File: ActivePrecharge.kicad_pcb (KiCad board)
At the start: 2 copper layers, 36 parts, among them J1 Conn_01x02, J2 Conn_01x03, J3 Conn_01x02, Q1 IRLML0030, U1 TCMT1106, U2 NCP785AH120T1G, U3 NCP785AH120T1G

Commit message: ACPR_Initial_Layout_Jacob
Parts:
- removed R1a1: 10k, Resistor_SMD:R_0805_2012Metric
- removed R6a1: 250, Resistor_SMD:R_0805_2012Metric
- C3, C5: footprint Capacitor_SMD:C_0805_2012Metric -> BigCap:CAPC5750X220N
- R1: renamed from R1b1; value 100k -> 110k; footprint Resistor_SMD:R_0805_2012Metric -> Resistor_SMD:R_1206_3216Metric
- R3: footprint Resistor_SMD:R_0805_2012Metric -> Resistor_SMD:R_1206_3216Metric
- R6b1: value 500 -> 750
- moved H4 126.5 mm to (85.8, 115.5)
- moved H2 80.8 mm to (139.5, 75.5)
- moved Q1 69.0 mm to (134.1, 108.4), turned to 90 degrees
- moved J3 65.9 mm to (138.8, 100.0), turned to -90 degrees
- moved D3 64.5 mm to (133.7, 77.5), turned to -90 degrees
- moved D1 62.4 mm to (133.5, 101.7), turned to -90 degrees
- moved R11 61.7 mm to (130.5, 110.2), turned to -90 degrees
- moved J1 57.6 mm to (138.7, 87.0), turned to -90 degrees
- moved PreResH1 56.3 mm to (85.8, 75.8)
- moved H3 55.6 mm to (139.5, 115.5)
- moved D2 52.4 mm to (133.8, 96.4), turned to 90 degrees
- moved R9 52.0 mm to (133.8, 92.4), turned to 90 degrees
- moved C2 48.0 mm to (133.7, 84.8), turned to -90 degrees
- moved C1 47.5 mm to (133.7, 88.5), turned to 90 degrees
- moved R10 46.5 mm to (133.7, 81.2), turned to 90 degrees
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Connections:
- J1 pad 1: +12V -> LVGND
- J1 pad 2: LVGND -> +12V
- J2 pad 1: /HVRef -> HVGND
- J2 pad 2: /HVIn -> /HVRef
- J2 pad 3: HVGND -> /HVIn
- R1 pad 1: Net-(R1a1-Pad2) -> /HVRef
- R6b1 pad 1: Net-(R6a1-Pad2) -> /Vcc
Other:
- board outline added: 64.2 x 50.5 mm

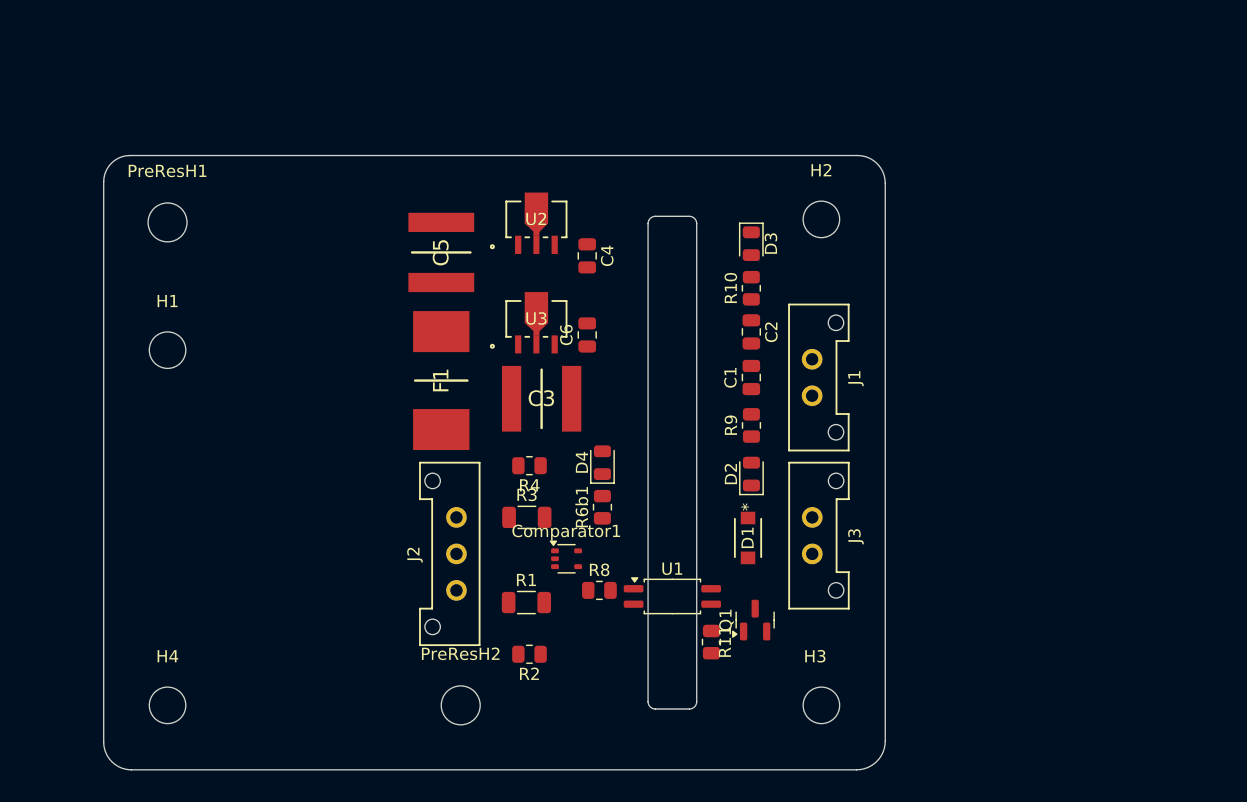
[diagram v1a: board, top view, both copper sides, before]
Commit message: schematic edits and layout prototype
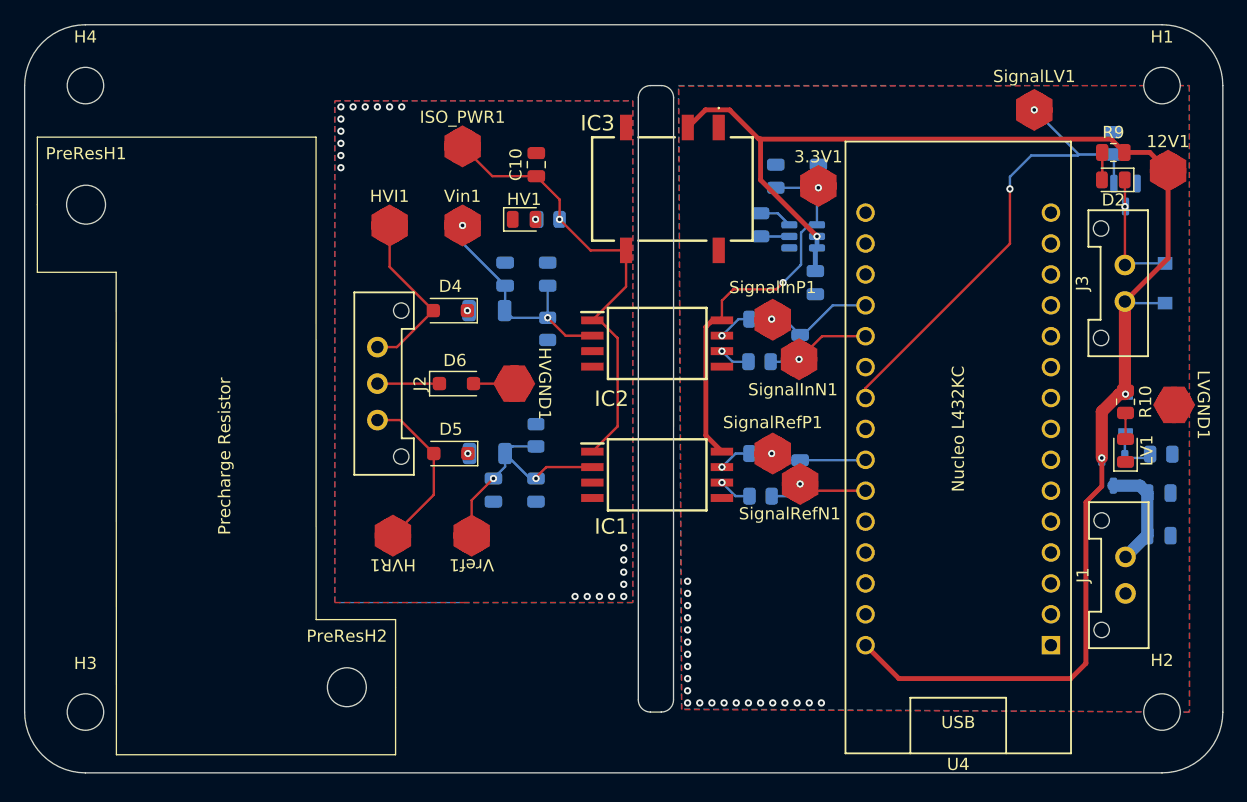
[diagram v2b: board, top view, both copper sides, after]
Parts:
- removed Comparator1: TLV9301xDCK, Package_TO_SOT_SMD:SOT-353_SC-70-5
- removed D3: LED, LED_SMD:LED_0805_2012Metric
- removed F1: 46205, 46205Fuse:FUSC10545X460N
- removed R6b1: 750, Resistor_SMD:R_0805_2012Metric
- removed U1: TCMT1106, Package_SO:SOP-4_4.4x2.6mm_P1.27mm
- removed U2: NCP785AH120T1G, LDO:SOT-89-3_2P7X4P7_ONS
- added 12V1: TestPoint, Active-PrechargeLib:TestPoint_HEX_3mmID, F.Cu at (168.0, 71.5)
- added 3.3V1: TestPoint, Active-PrechargeLib:TestPoint_HEX_3mmID, F.Cu at (139.2, 72.8)
- added C10: 0.1u, Capacitor_SMD:C_0805_2012Metric, F.Cu at (116.1, 71.0)
- added C12: 10n, Capacitor_SMD:C_0805_2012Metric, B.Cu at (137.8, 96.2)
- added C13: 100n, Capacitor_SMD:C_0805_2012Metric, B.Cu at (139.2, 72.0)
- added C15: 1uF, Capacitor_SMD:C_0805_2012Metric, B.Cu at (113.5, 80.0)
- added C7: 1uF, Capacitor_SMD:C_0805_2012Metric, B.Cu at (112.5, 97.8)
- added C8: 10n, Capacitor_SMD:C_0805_2012Metric, B.Cu at (137.8, 86.0)
- added C9: 100p, Capacitor_SMD:C_0805_2012Metric, B.Cu at (116.0, 97.8)
- added D5: RSX068MP2STR, Diode_SMD:D_SOD-123F, F.Cu at (109.0, 94.8)
- added D6: RSX068MP2STR, Diode_SMD:D_SOD-123F, F.Cu at (109.5, 89.0)
- added D7: BZT52-B12-QX, Active-PrechargeLib:BZT52B12QX, B.Cu at (164.5, 91.5)
- added HV1: LED, LED_SMD:LED_0805_2012Metric, F.Cu at (115.1, 75.5)
- added HVGND1: TestPoint, Active-PrechargeLib:TestPoint_HEX_3mmID, F.Cu at (114.2, 89.0)
- added HVI1: TestPoint, Active-PrechargeLib:TestPoint_HEX_3mmID, F.Cu at (104.0, 76.0)
- added HVR1: TestPoint, Active-PrechargeLib:TestPoint_HEX_3mmID, F.Cu at (104.3, 101.5)
- added IC1: AMC1311BDWVR, AMC1311:SOIC127P1150X280-8N, F.Cu at (126.0, 96.5)
- added IC2: AMC1311BDWVR, AMC1311:SOIC127P1150X280-8N, F.Cu at (126.0, 85.7)
- added IC3: 1769205241, Active-PrechargeLib:1769205241, F.Cu at (127.2, 73.0)
- added ISO_PWR1: TestPoint, utsvt-special:TestPoint_HEX_3mmID, F.Cu at (110.0, 69.5)
- added LV1: LED, LED_SMD:LED_0805_2012Metric, F.Cu at (164.5, 94.5)
- added LVGND1: TestPoint, Active-PrechargeLib:TestPoint_HEX_3mmID, F.Cu at (168.5, 90.8)
- added Q2: PMV35EPER, Package_TO_SOT_SMD:SOT-23-3, B.Cu at (163.5, 96.2)
- added R12: 100k, Resistor_SMD:R_0805_2012Metric, B.Cu at (167.4, 94.8)
- added R13: 640, Resistor_SMD:R_0805_2012Metric, B.Cu at (117.1, 75.5)
- added R5: 10, Resistor_SMD:R_0805_2012Metric, B.Cu at (134.5, 83.7)
- added R6: 10, Resistor_SMD:R_0805_2012Metric, B.Cu at (134.4, 87.2)
- added R7: 10, Resistor_SMD:R_0805_2012Metric, B.Cu at (134.5, 94.8)
- added SignalInN1: TestPoint, Active-PrechargeLib:TestPoint_HEX_3mmID, F.Cu at (137.7, 87.0)
- added SignalInP1: TestPoint, Active-PrechargeLib:TestPoint_HEX_3mmID, F.Cu at (135.5, 83.8)
- added SignalLV1: TestPoint, Active-PrechargeLib:TestPoint_HEX_3mmID, F.Cu at (157.0, 66.5)
- added SignalRefN1: TestPoint, Active-PrechargeLib:TestPoint_HEX_3mmID, F.Cu at (137.8, 97.2)
- added SignalRefP1: TestPoint, Active-PrechargeLib:TestPoint_HEX_3mmID, F.Cu at (135.5, 94.8)
- added U4: Nucleo_L432KC, utsvt-special:NucleoL432KC, F.Cu at (150.8, 92.7)
- added Vin1: TestPoint, Active-PrechargeLib:TestPoint_HEX_3mmID, F.Cu at (110.0, 76.0)
- added Vref1: TestPoint, Active-PrechargeLib:TestPoint_HEX_3mmID, F.Cu at (110.8, 101.5)
- C1, C2: value 100u -> 10u; moved to B.Cu
- C3: value 2.2u -> 100p; footprint BigCap:CAPC5750X220N -> Capacitor_SMD:C_0805_2012Metric; moved to B.Cu
- C4: value 22u -> 100n; moved to B.Cu
- C5: value 2.2u -> 44u; footprint BigCap:CAPC5750X220N -> Capacitor_SMD:C_0805_2012Metric; moved to B.Cu
- C6: value 22u -> 10u; moved to B.Cu
- D1, Q1, R11, R3: moved to B.Cu
- D4: value LED -> RSX068MP2STR; footprint LED_SMD:LED_0805_2012Metric -> Diode_SMD:D_SOD-123F
- R1: value 110k -> 100k; moved to B.Cu
- R10: value 5k -> 2k
- R2, R4: value 1k -> 2k; moved to B.Cu
- R8: value 250 -> 10; moved to B.Cu
- U3: value NCP785AH120T1G -> AP63203WU; footprint LDO:SOT-89-3_2P7X4P7_ONS -> Package_TO_SOT_SMD:TSOT-23-6; moved to B.Cu
- moved H1 84.6 mm to (167.5, 64.5)
- moved H3 60.5 mm to (79.0, 116.0)
- moved R11 52.7 mm to (163.5, 69.2), turned to 90 degrees
- moved H4 51.4 mm to (79.0, 64.5)
- moved H2 49.2 mm to (167.5, 116.0)
- moved Q1 46.3 mm to (164.5, 73.5), turned to -90 degrees
- moved D1 40.2 mm to (167.8, 80.8), turned to 90 degrees
- moved D2 38.3 mm to (163.5, 72.2), turned to 180 degrees
- moved R9 37.3 mm to (163.5, 70.0), turned to 0 degrees
- moved C2 36.0 mm to (167.2, 98.0), turned to 0 degrees
- moved C1 35.9 mm to (167.2, 101.5), turned to 0 degrees
- moved J1 32.2 mm to (164.5, 106.2), turned to 90 degrees
- moved R10 32.1 mm to (164.5, 90.5), turned to -90 degrees
- moved J3 31.2 mm to (164.4, 82.2), turned to 90 degrees
- moved C5 28.2 mm to (135.8, 72.0)
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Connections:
- C3 pad 1: Net-(U2-IN) -> /HVGND
- C3 pad 2: HVGND -> /Vin
- C4 pad 1: /Vcc -> Net-(U3-SW)
- C4 pad 2: HVGND -> Net-(U3-BST)
- C5 pad 1: Net-(U2-IN) -> /3.3V
- C5 pad 2: HVGND -> LVGND
- C6 pad 1: /Vcc -> LVGND
- C6 pad 2: HVGND -> /LV+
- D1 pad 1: +12V -> /LV+
- D4 pad 1: HVGND -> /HVIn
- D4 pad 2: Net-(D4-A) -> /HIn
- J2 pad 1: HVGND -> /HIn
- J2 pad 2: /HVRef -> HGND
- J2 pad 3: /HVIn -> HRef
- J3 pad 1: +12V -> /LV+
- R10 pad 1: +12V -> /LV+
- R2 pad 2: HVGND -> /HVGND
- R4 pad 2: HVGND -> /HVGND
- R8 pad 1: /SignalHV -> Net-(IC1-VOUTN)
- R8 pad 2: Net-(R8-Pad2) -> /SignalRefN
- R9 pad 2: +12V -> /LV+
- U3 pad 1: Net-(U2-IN) -> /3.3V
- U3 pad 2: HVGND -> /LV+
- U3 pad 3: /Vcc -> /LV+
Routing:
- net /LV+: track 0.00 -> 121.5 mm, vias 0 -> 3
- net /SignalLV: track 0.00 -> 40.0 mm, vias 0 -> 2
- net /ISO_PWR: track 0.00 -> 37.7 mm, vias 0 -> 1
- net /3.3V: track 0.00 -> 32.5 mm, vias 0 -> 2
- net /Vin: track 0.00 -> 19.2 mm, vias 0 -> 2
- net /Vref: track 0.00 -> 19.1 mm, vias 0 -> 2
- net /HIn: track 0.00 -> 14.3 mm
- net HRef: track 0.00 -> 13.9 mm
- net Net-(D1-A): track 0.00 -> 10.4 mm, vias 0 -> 1
- net /SignalInP: track 0.00 -> 9.26 mm, vias 0 -> 1
- net +12V: track 0.00 -> 9.13 mm
- net /SignalInN: track 0.00 -> 8.67 mm, vias 0 -> 1
- net /SignalRefN: track 0.00 -> 8.38 mm, vias 0 -> 1
- net /SignalRefP: track 0.00 -> 7.96 mm, vias 0 -> 1
- net HGND: track 0.00 -> 5.10 mm
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- added copper zone on B.Cu, net /HVGND
- added copper zone on F.Cu, net /HVGND
- added copper zone on B.Cu, net LVGND
- added copper zone on F.Cu, net LVGND
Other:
- board size 64.2 x 50.5 mm -> 98.5 x 61.5 mm
- board text added: "Precharge Resistor"

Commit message: balancing
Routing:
- net /3.3V: track 32.5 -> 33.9 mm
- net LVGND: vias 22 -> 29
- net /HVGND: vias 20 -> 29
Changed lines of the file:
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@@
+	)
+	(via
+		(at 156.5 109.25)
+		(size 0.6)
+		(drill 0.3)
+		(layers "F.Cu" "B.Cu")
+		(free yes)
+		(net 2)
 	)
 	(via
@@
 	)
 	(via
+		(at 156.5 107.25)
+		(size 0.6)
+		(drill 0.3)
+		(layers "F.Cu" "B.Cu")
+		(free yes)
+		(net 2)
+	)
+	(via
 		(at 128.5 113.25)
 		(size 0.6)
@@
 	)
 	(via
+		(at 156.5 108.25)
+		(size 0.6)
+		(drill 0.3)
+		(layers "F.Cu" "B.Cu")
+		(free yes)
+		(net 2)
+	)
+	(via
 		(at 128.5 108.25)
 		(size 0.6)
@@
 	)
 	(via
+		(at 156.5 105.25)
+		(size 0.6)
+		(drill 0.3)
+		(layers "F.Cu" "B.Cu")
+		(free yes)
+		(net 2)
+	)
+	(via
 		(at 132.5 115.25)
 		(size 0.6)
@@
 	)
 	(via
+		(at 156.5 106.25)
+		(size 0.6)
+		(drill 0.3)
+		(layers "F.Cu" "B.Cu")
+		(free yes)
+		(net 2)
+	)
+	(via
+		(at 156.5 111.25)
+		(size 0.6)
+		(drill 0.3)
+		(layers "F.Cu" "B.Cu")
+		(free yes)
+		(net 2)
+	)
+	(via
 		(at 130.5 115.25)
 		(size 0.6)
@@
 	(via
 		(at 136.5 115.25)
+		(size 0.6)
+		(drill 0.3)
+		(layers "F.Cu" "B.Cu")
+		(free yes)
+		(net 2)
+	)
+	(via
+		(at 156.5 110.25)
 		(size 0.6)
 		(drill 0.3)
@@
 	)
 	(via
+		(at 100 106.5)
+		(size 0.6)
+		(drill 0.3)
+		(layers "F.Cu" "B.Cu")
+		(free yes)
+		(net 11)
+	)
+	(via
 		(at 100 69.25)
 		(size 0.6)
@@
 	)
 	(via
+		(at 102 106.5)
+		(size 0.6)
+		(drill 0.3)
+		(layers "F.Cu" "B.Cu")
+		(free yes)
+		(net 11)
+	)
+	(via
 		(at 100 66.25)
 		(size 0.6)
@@
 	)
 	(via
+		(at 100 103.5)
+		(size 0.6)
+		(drill 0.3)
+		(layers "F.Cu" "B.Cu")
+		(free yes)
+		(net 11)
+	)
+	(via
+		(at 100 102.5)
+		(size 0.6)
+		(drill 0.3)
+		(layers "F.Cu" "B.Cu")
+		(free yes)
+		(net 11)
+	)
+	(via
+		(at 100 105.5)
+		(size 0.6)
+		(drill 0.3)
+		(layers "F.Cu" "B.Cu")
+		(free yes)
+		(net 11)
+	)
+	(via
 		(at 104 66.25)
 		(size 0.6)
@@
 	)
 	(via
+		(at 103 106.5)
+		(size 0.6)
+		(drill 0.3)
+		(layers "F.Cu" "B.Cu")
+		(free yes)
+		(net 11)
+	)
+	(via
 		(at 119.25 106.5)
 		(size 0.6)
@@
 	)
 	(via
+		(at 104 106.5)
+		(size 0.6)
+		(drill 0.3)
+		(layers "F.Cu" "B.Cu")
+		(free yes)
+		(net 11)
+	)
+	(via
 		(at 102 66.25)
 		(size 0.6)
@@
 	)
 	(via
+		(at 101 106.5)
+		(size 0.6)
+		(drill 0.3)
+		(layers "F.Cu" "B.Cu")
+		(free yes)
+		(net 11)
+	)
+	(via
 		(at 123.25 106.5)
 		(size 0.6)
@@
 	(via
 		(at 121.25 106.5)
+		(size 0.6)
+		(drill 0.3)
+		(layers "F.Cu" "B.Cu")
+		(free yes)
+		(net 11)
+	)
+	(via
+		(at 100 104.5)
 		(size 0.6)
 		(drill 0.3)
@@
 	)
 	(segment
-		(start 130 84.34)
-		(end 130 93.27)
-		(width 0.4)
-		(layer "F.Cu")
-		(net 14)
-	)
-	(segment
 		(start 132.25 81.25)
 		(end 131.325 82.175)
@@
 	)
 	(segment
-		(start 130.545 83.795)
-		(end 130 84.34)
-		(width 0.4)
-		(layer "F.Cu")
-		(net 14)
-	)
-	(segment
 		(start 131.325 82.175)
 		(end 131.325 83.795)
@@
 	)
 	(segment
+		(start 130.055 83.795)
+		(end 128.7 85.15)
+		(width 0.2)
+		(layer "F.Cu")
+		(net 14)
+	)
+	(segment
+		(start 128.7 91.97)
+		(end 131.325 94.595)
+		(width 0.2)
+		(layer "F.Cu")
+		(net 14)
+	)
+	(segment
+		(start 128.7 85.15)
+		(end 128.7 91.97)
+		(width 0.2)
+		(layer "F.Cu")
+		(net 14)
+	)
+	(segment
 		(start 136.35 80.7)
 		(end 135.8 81.25)
@@
 	)
 	(segment
-		(start 130 93.27)
-		(end 131.325 94.595)
-		(width 0.4)
+		(start 131.325 83.795)
+		(end 130.055 83.795)
+		(width 0.2)
 		(layer "F.Cu")
 		(net 14)
-	)
-	(segment
-		(start 131.325 83.795)
-		(end 130.545 83.795)
-		(width 0.4)
-		(layer "F.Cu")
-		(net 14)

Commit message: layout revisions inital draft finished
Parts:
- C10: moved to B.Cu
- R13: moved to F.Cu
- moved HVGND1 15.5 mm to (113.5, 104.5), turned to 180 degrees
- moved C3 8.05 mm to (113.5, 87.2), turned to 90 degrees
- moved C4 8.00 mm to (126.6, 74.6)
- moved C5 8.00 mm to (127.9, 70.6)
- moved C12 7.73 mm to (130.1, 97.2)
- moved R7 7.73 mm to (126.8, 95.8)
- moved R8 7.73 mm to (126.8, 99.2)
- moved C13 7.68 mm to (131.9, 69.8)
- moved C6 7.68 mm to (131.6, 78.6)
- moved U3 7.68 mm to (130.6, 74.8)
- moved 3.3V1 7.58 mm to (131.9, 70.9)
- moved C8 7.51 mm to (130.2, 86.3)
- moved R5 7.51 mm to (127.0, 84.0)
- moved R6 7.51 mm to (126.9, 87.5)
- moved SignalInN1 7.51 mm to (130.2, 87.3)
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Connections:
- D6 pad 2: Net-(D6-A) -> /HVGND
- HVGND1 pad 1: Net-(D6-A) -> /HVGND
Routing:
- net /LV+: track 121.5 -> 111.1 mm
- net /SignalRefN: track 8.38 -> 18.6 mm, vias 1 -> 0
- net Net-(D1-A): track 10.4 -> 15.7 mm, vias 1 -> 0
- net /SignalLV: track 40.0 -> 34.8 mm, vias 2 -> 1
- net +12V: track 9.13 -> 12.9 mm
- net /3.3V: track 33.9 -> 37.4 mm, vias 2 -> 1
- net Net-(D6-A): track 3.35 -> 0.00 mm
- net Net-(D7-A): track 3.93 -> 5.75 mm
- net /ISO_PWR: track 37.7 -> 36.0 mm
- net Net-(HV1-A): track 0.00 -> 1.65 mm, vias 1 -> 0
- net /SignalRefP: track 7.96 -> 9.59 mm
- net Net-(IC2-VOUTP): track 2.83 -> 1.38 mm
- net Net-(IC1-VOUTP): track 2.72 -> 1.36 mm
- net Net-(IC1-VOUTN): track 2.72 -> 1.36 mm
- net /SignalInP: track 9.26 -> 10.5 mm
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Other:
- board size 98.5 x 61.5 mm -> 93.5 x 61.5 mm

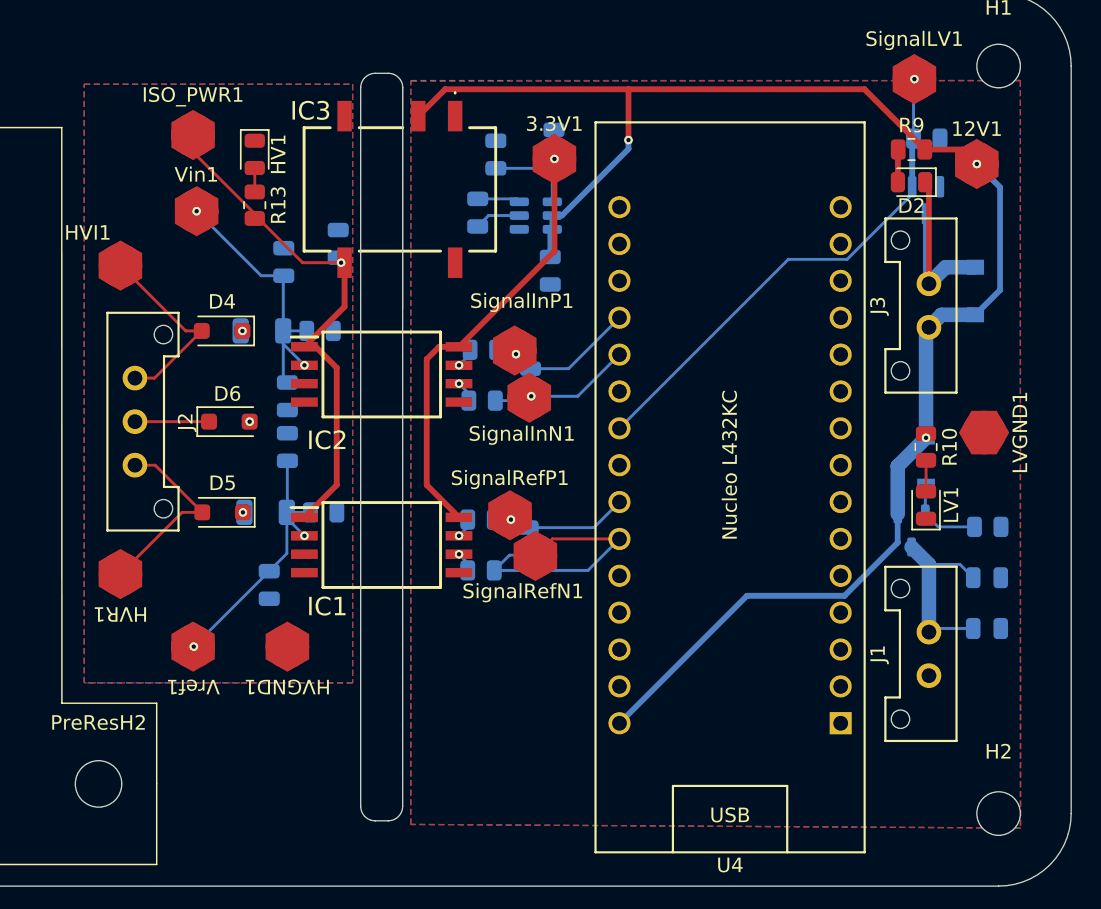
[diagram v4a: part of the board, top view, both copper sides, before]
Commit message: added stitching vias and fixed silkscreen warnings
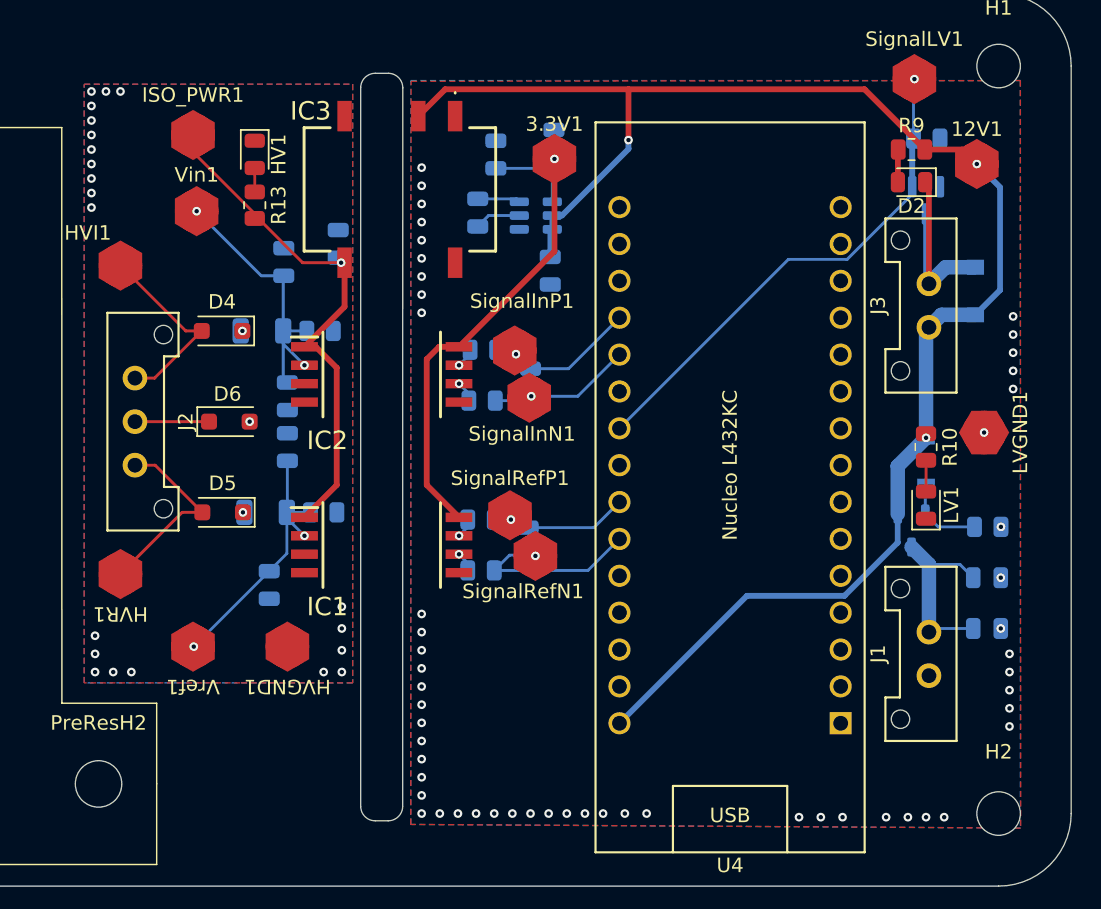
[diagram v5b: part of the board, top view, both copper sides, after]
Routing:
- net /SignalRefN: track 18.6 -> 12.3 mm, vias 0 -> 1
- net LVGND: vias 0 -> 54
- net /HVGND: vias 1 -> 22
